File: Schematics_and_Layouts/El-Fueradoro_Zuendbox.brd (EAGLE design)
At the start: 157.5 x 97.5 mm, 140 parts, among them IC1 MAX202, IC2 MEGA168P/328P, IC4 MC33063-DIL, IC6 74HC595N, IC7 74HC595N, IC8 LD117AV, Q1 9.8304, Q10 IRF3708, Q11 IRF3708, Q12 IRF3708, Q13 IRF3708, Q14 IRF3708, Q15 IRF3708, Q16 IRF3708, Q17 IRF3708, Q2 IRF3708, Q3 IRF3708, Q4 IRF3708, Q5 IRF3708, Q6 IRF3708, Q7 IRF3708, Q8 IRF3708, Q9 IRF3708

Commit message: Added size-information-output for Hexfiles/build_hexfiles.bat Extended manual and added BOMs BOM-Update (final one, hopefully!)
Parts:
- R12, R38: value 4k7 -> 3k3
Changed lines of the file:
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@@
 <attribute name="VALUE" x="150.495" y="64.389" size="1.27" layer="27" ratio="10"/>
 </element>
-<element name="R12" library="rcl" package="0207/10" value="4k7" x="96.52" y="63.5" smashed="yes" rot="R90">
+<element name="R12" library="rcl" package="0207/10" value="3k3" x="96.52" y="63.5" smashed="yes" rot="R90">
 <attribute name="NAME" x="96.901" y="62.357" size="1" layer="25" font="vector" ratio="10" rot="R90"/>
 <attribute name="VALUE" x="97.155" y="61.2394" size="1" layer="27" font="vector" ratio="10" rot="R90"/>
@@
 <attribute name="VALUE" x="83.312" y="7.62" size="1" layer="27" font="vector" ratio="10" rot="R90"/>
 </element>
-<element name="R38" library="rcl" package="0207/10" value="4k7" x="55.88" y="10.16" smashed="yes" rot="R180">
+<element name="R38" library="rcl" package="0207/10" value="3k3" x="55.88" y="10.16" smashed="yes" rot="R180">
 <attribute name="NAME" x="57.3405" y="10.541" size="1" layer="25" font="vector" ratio="10" rot="R180"/>
 <attribute name="VALUE" x="58.1406" y="10.795" size="1" layer="27" font="vector" ratio="10" rot="R180"/>

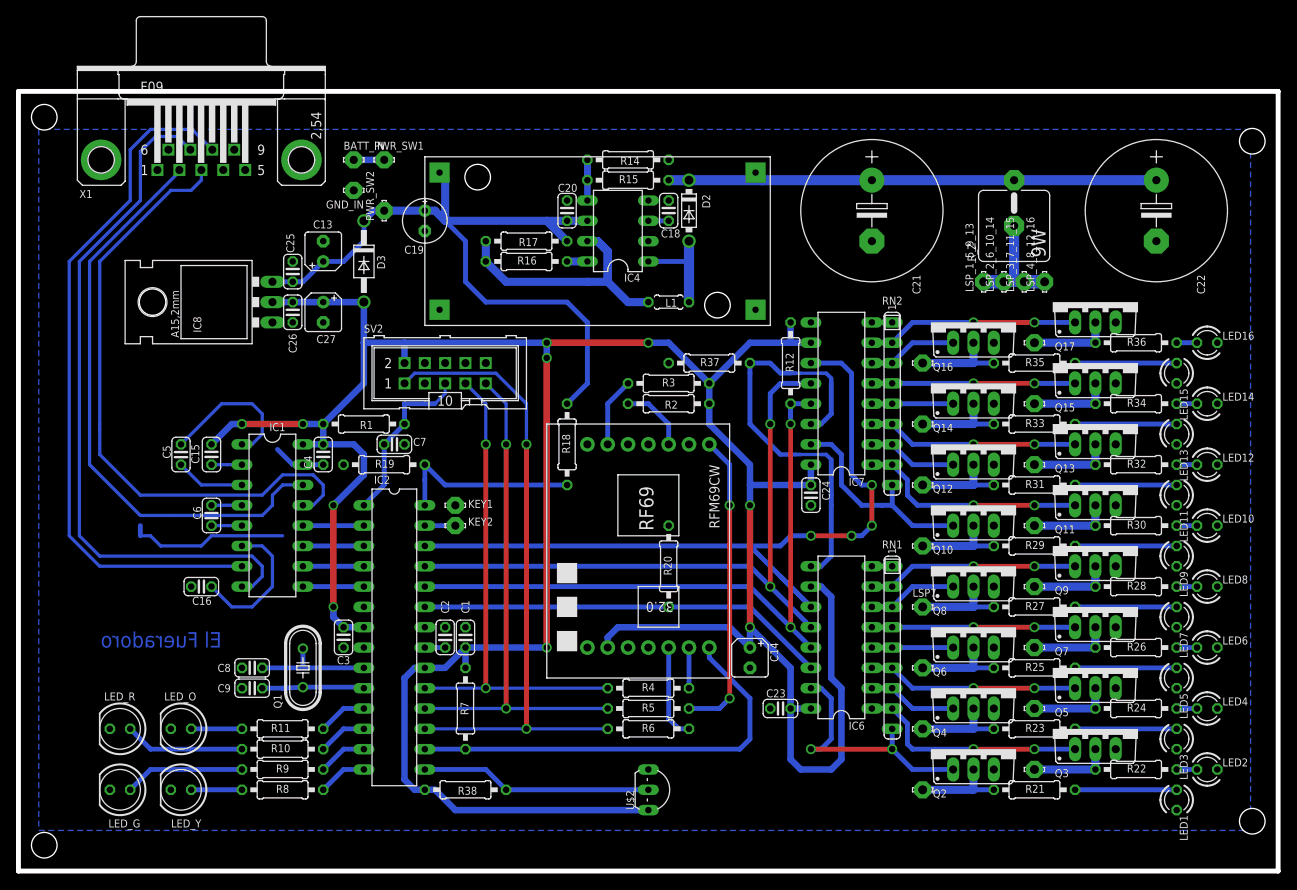
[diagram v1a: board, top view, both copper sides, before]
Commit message: Layout fixes Additions to manual once again
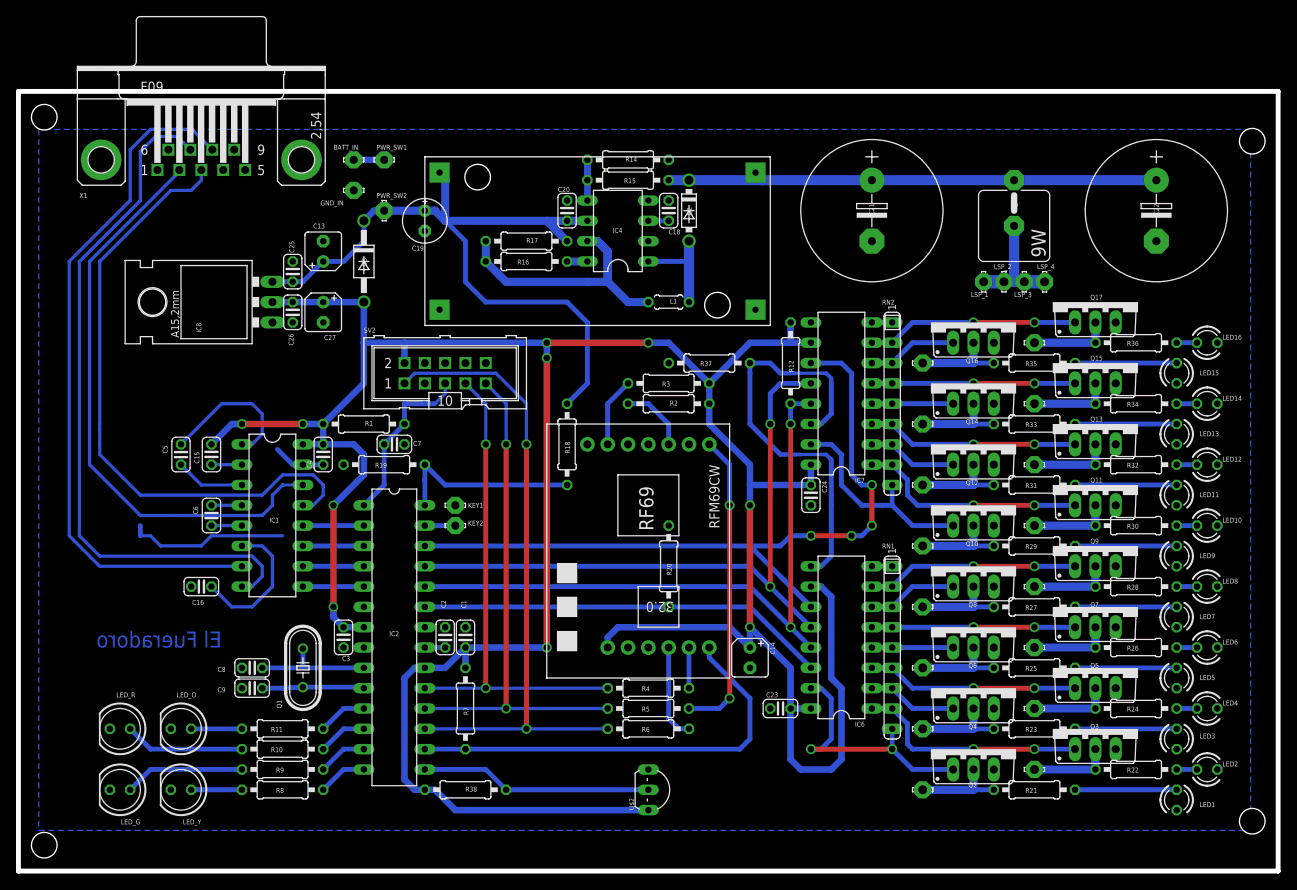
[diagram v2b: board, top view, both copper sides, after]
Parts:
- IC8: value LD117AV -> LM1086IT-3.3
- renumbered LSP_1_5_9_13 to LSP_1, LSP_2_6_10_14 to LSP_2, LSP_3_7_11_15 to LSP_3, LSP_4_8_12_16 to LSP_4
